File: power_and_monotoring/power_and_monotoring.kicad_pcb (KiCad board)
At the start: 2 copper layers, 122 x 124.4 mm, 159 parts, among them IC1 ADP3335ARMZ-5-R7, IC2 ADP3335ARMZ-3.3-RL, IC3 LM2576-12WU-TR, J1 Microfit_01x02_Vertical, J2 HLE-108-02-L-DV-BE-K-TR, J3 HLE-108-02-L-DV-BE-K-TR, J4 HLE-108-02-L-DV-BE-K-TR, J5 HLE-108-02-L-DV-BE-K-TR, J6 43045-1015, J7 43045-1615, K1 G5Q-1A, K2 G5Q-1A, K3 G5Q-1A, Q1 DMN6075SQ-7, U1 74LVC1G08GW,125, U11 CD4051BM96G3, U12 CD4051BM96G3, U2 LM7902D, U3 LM7902D, U4 LM7902D, U7 CD4071BM96

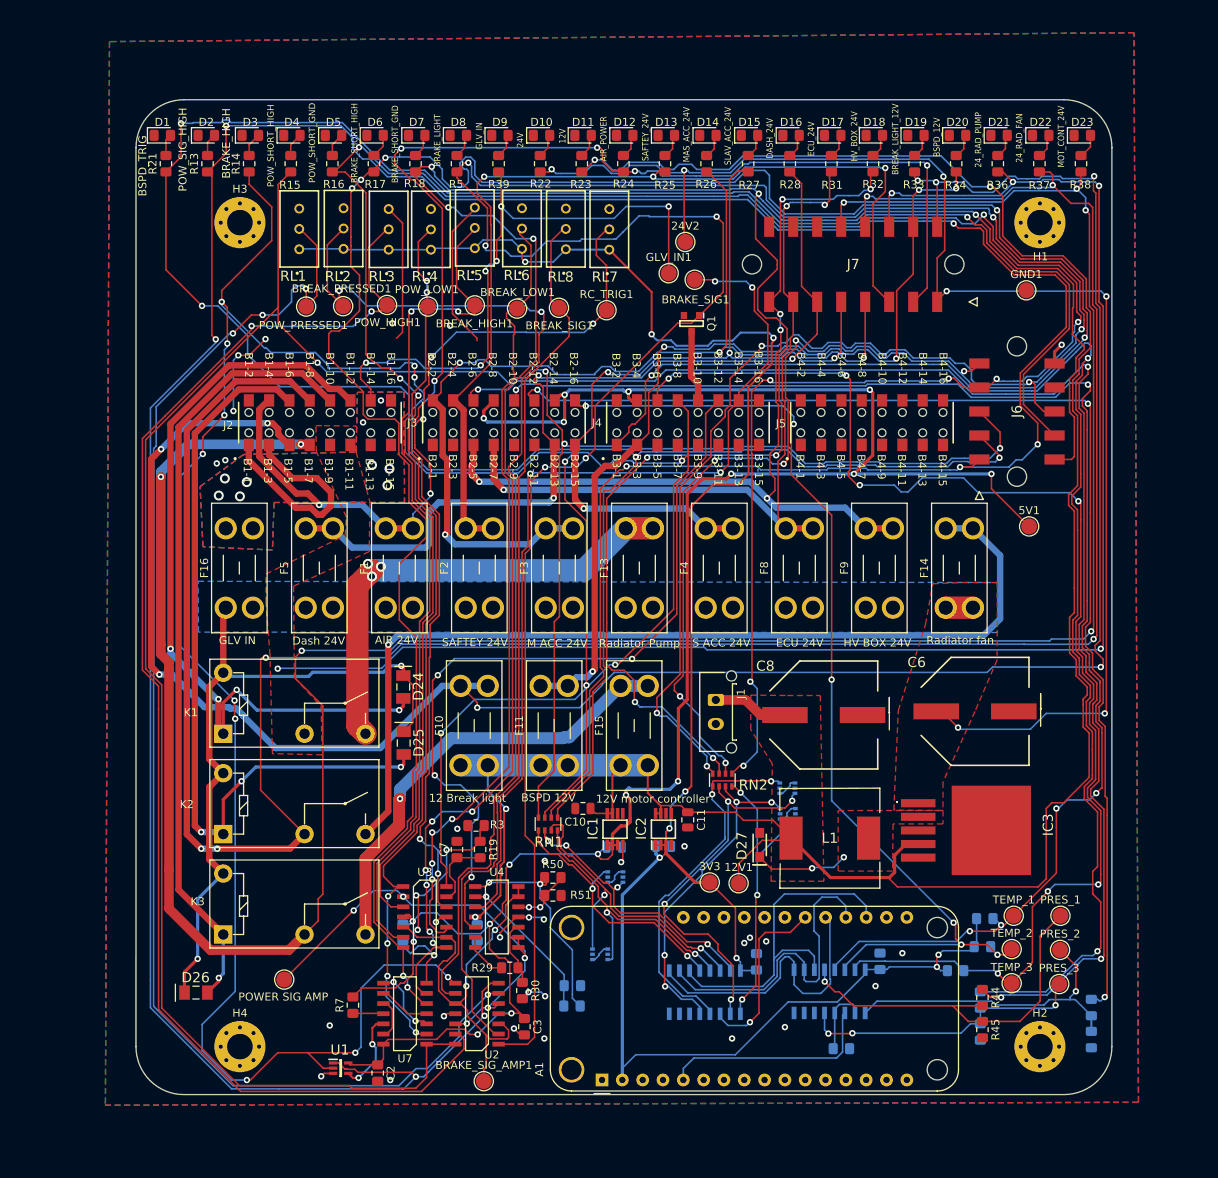
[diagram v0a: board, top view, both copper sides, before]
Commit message: Made it 4 layers
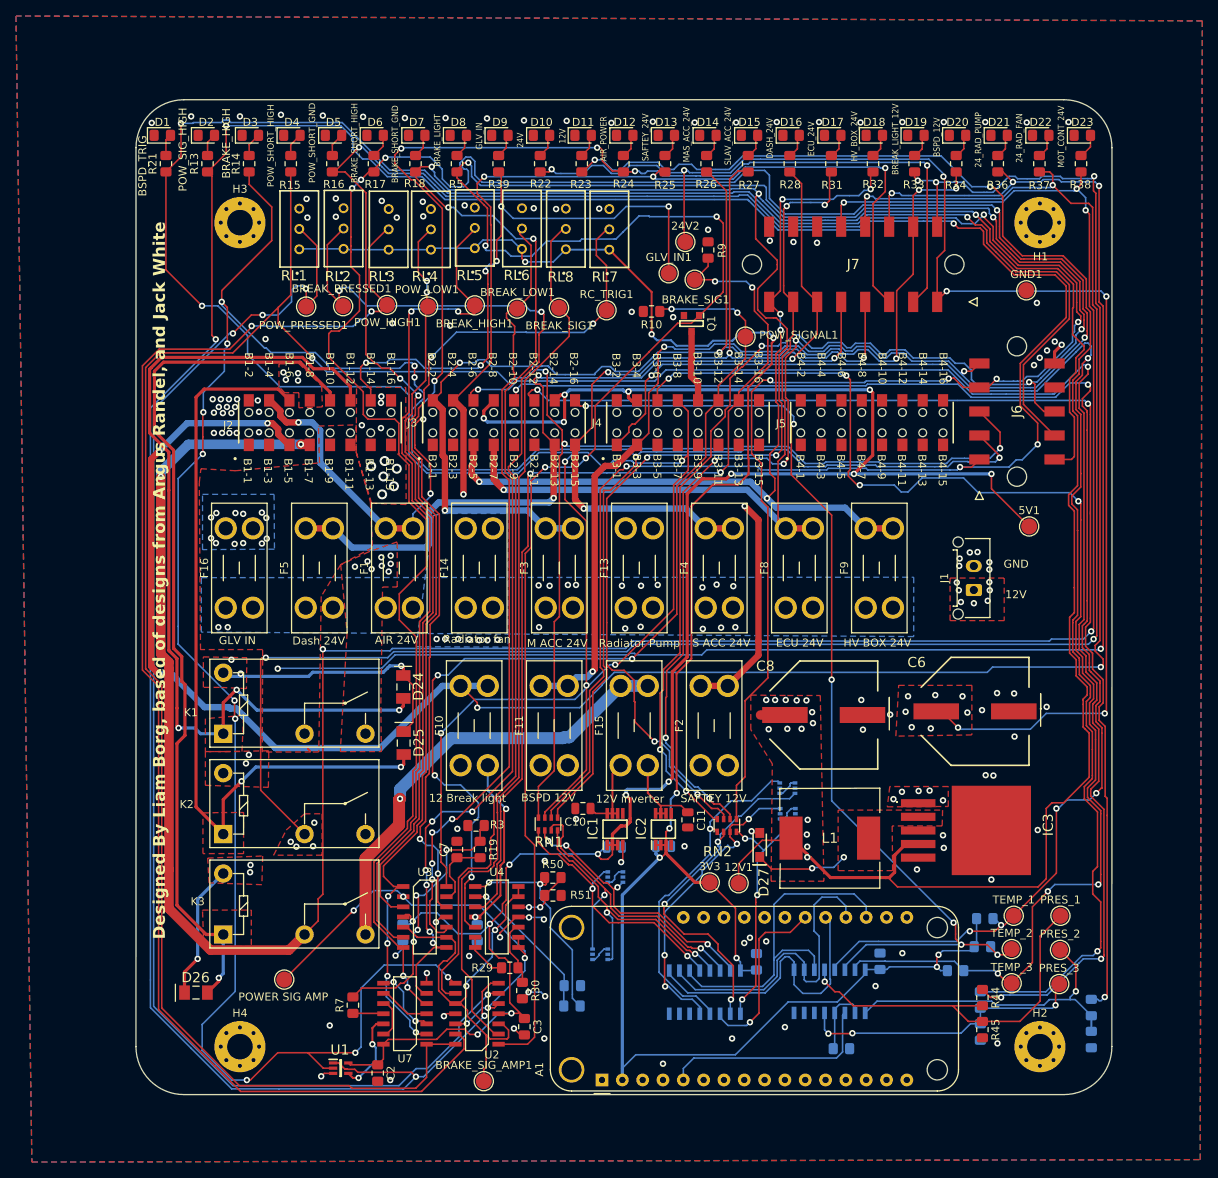
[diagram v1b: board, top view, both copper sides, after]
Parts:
- added POW_SIGNAL1: TestPoint, TestPoint:TestPoint_Pad_D2.0mm, F.Cu at (117.5, 159.4)
- added R10: CRCW0805, UniSA_Motorsport_Resistor:0805, F.Cu at (105.8, 156.3)
- added R9: CRCW0805, UniSA_Motorsport_Resistor:0805, F.Cu at (112.8, 148.6)
- moved F14 60.0 mm to (82.5, 193.3)
- moved F2 35.4 mm to (111.9, 213.0)
- moved J1 35.1 mm to (146.0, 191.1), turned to 90 degrees
- moved RN2 5.70 mm to (115.2, 220.5)
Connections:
- net Net-(F13-Pad2) renamed /fuses/PUMP_FUSE_RELAY
- F2 pad 1: +24V -> +12V
- IC1 pad 6: unconnected-(IC1-~{SD}-Pad6) -> +12V
- IC2 pad 6: unconnected-(IC2-~{SD}-Pad6) -> +12V
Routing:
- net Net-(F14-Pad2): track 118.8 -> 0.00 mm, vias 1 -> 7
- net /Connectors/RADIATOR_FAN_24V: track 306.5 -> 220.8 mm, vias 6 -> 12
- net GND: track 118.0 -> 36.9 mm, vias 32 -> 118
- net /fuses/PUMP_FUSE_RELAY: track 58.9 -> 0.00 mm, vias 3 -> 8
- net /Connectors/SAFETY_24V: track 122.0 -> 179.8 mm, vias 3 -> 5
- net +12V: track 298.7 -> 256.2 mm, vias 4 -> 25
- net /Connectors/POWER_SIGNAL: track 98.7 -> 121.5 mm, vias 4 -> 6
- net /Connectors/PUMP_ON_SIGNAL: track 98.2 -> 111.3 mm, vias 4 -> 3
- net +24V: track 265.5 -> 278.3 mm, vias 9 -> 45
- net /Connectors/MOTOR_CONTROLLER_ON_SIGNAL: track 97.0 -> 109.1 mm
- net /feather/BRAKE_SIG_AMP_SHORT_HIGH: track 355.1 -> 362.4 mm
- net Net-(U11-X4): track 37.7 -> 31.6 mm
- net /feather/POWER_SIG_SHORT_GND: track 331.0 -> 337.1 mm, vias 14 -> 12
- net /feather/POWER_SIG_SHORT_HIGH: track 318.4 -> 323.7 mm
- net /feather/BRAKE_LIGHT_SIG: track 377.1 -> 382.4 mm
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- added copper zone on In2.Cu, net +12V
- added copper zone on In2.Cu, net +24V
- added copper zone on In2.Cu, net /Connectors/GLV_MASTER_SWITCH_OUT
- added copper zone on F.Cu, net /Connectors/MOTOR_CONTROLLER_ON_SIGNAL
- added copper zone on F.Cu, net /Connectors/PUMP_ON_SIGNAL
- added copper zone on F.Cu, net /Connectors/RADIATOR_FAN_24V
- added copper zone on In2.Cu, net /Connectors/RADIATOR_FAN_24V
- added copper zone on F.Cu, net /Connectors/RADIATOR_FAN_ON_SIGNAL
- added copper zone on F.Cu, net /fuses/PUMP_FUSE_RELAY
- added copper zone on In2.Cu, net /fuses/PUMP_FUSE_RELAY
- added copper zone on In1.Cu, net GND
- added copper zone on B.Cu, net Net-(F14-Pad2)
- added copper zone on In2.Cu, net Net-(F14-Pad2)
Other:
- copper layers 2 -> 4
- board text added: "#bringBackCheesyCheeseBurgersFromHJs"
- board text added: "12V inverter"
- board text added: "Designed By Liam Borg, based of designs from Angus Randel, and Jack White"
- board text added: "GND"
- board text added: "Grand Lizzard Wizzard Liam"
- board text added: "I am witterally GOATed"
- board text added: "SAFTEY 12V"
- board text removed: "12V motor controller"
- board text removed: "SAFTEY 24V"
